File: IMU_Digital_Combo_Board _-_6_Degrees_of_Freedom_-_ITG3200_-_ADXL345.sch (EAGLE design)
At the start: 15 parts, among them U1 ADXL345, U3 ITG-32001:1

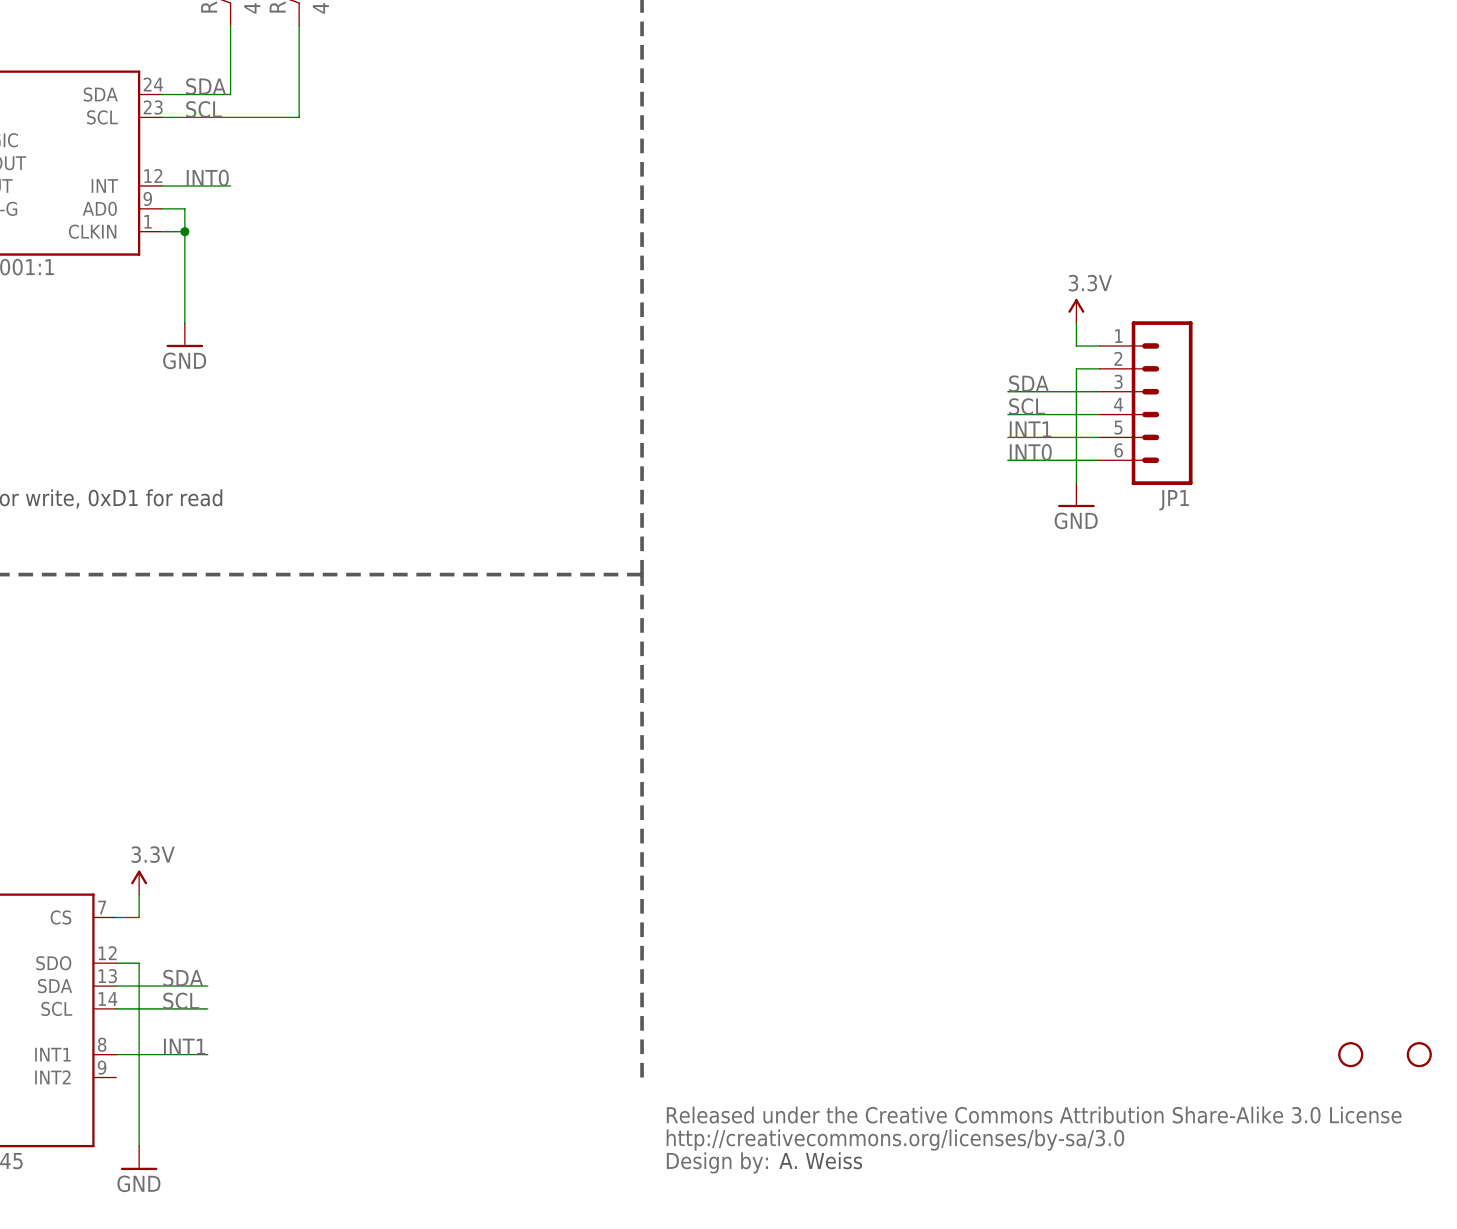
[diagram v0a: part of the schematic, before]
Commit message: Added production fiducials
Added:
- production fiducials
- flags in schematic for net labels
- modified two traces for better signal integrity
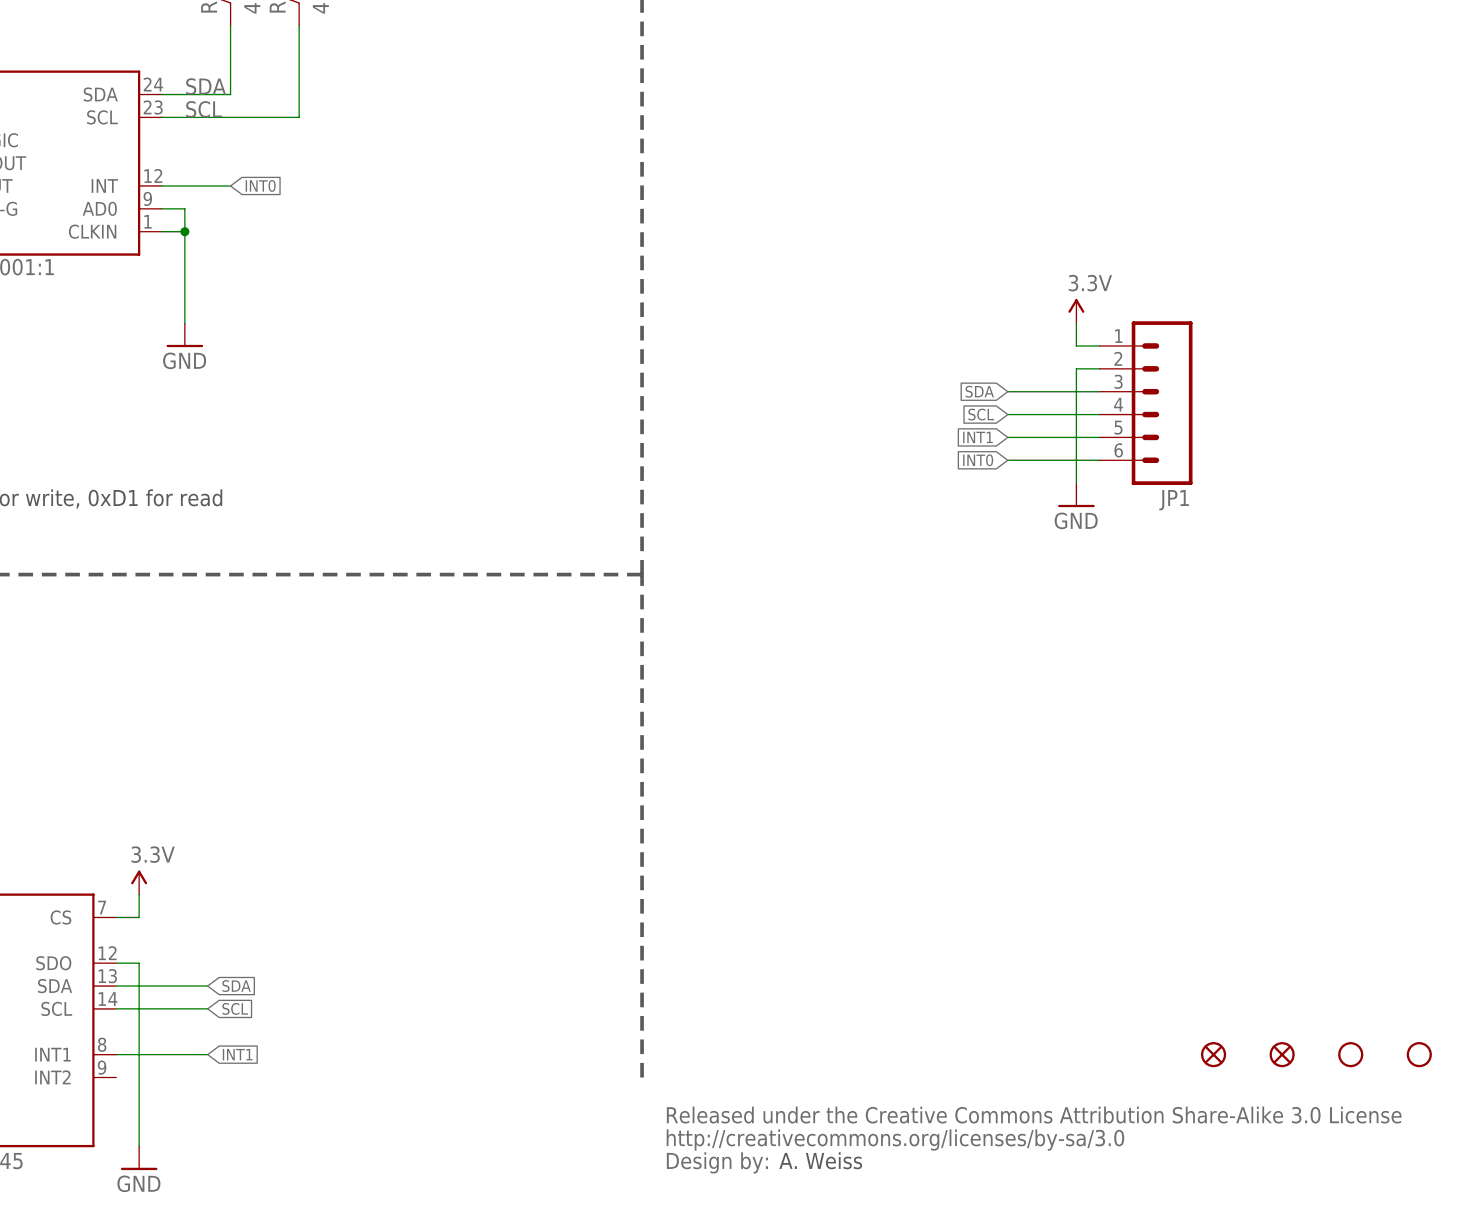
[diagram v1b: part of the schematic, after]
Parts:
- added JP4, JP6: FIDUCIAL1X2, SparkFun:FIDUCIAL1X2
